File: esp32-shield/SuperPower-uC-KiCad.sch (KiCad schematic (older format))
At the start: 3 parts, among them J9 MCU board

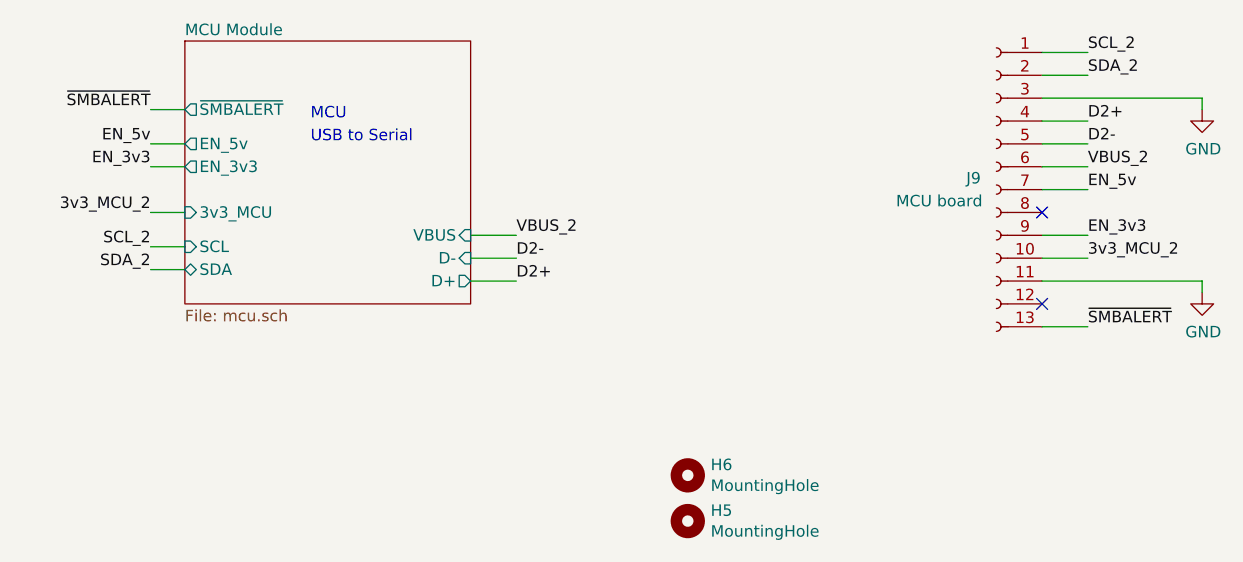
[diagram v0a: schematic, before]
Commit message: deleted unused files and renamed net lables
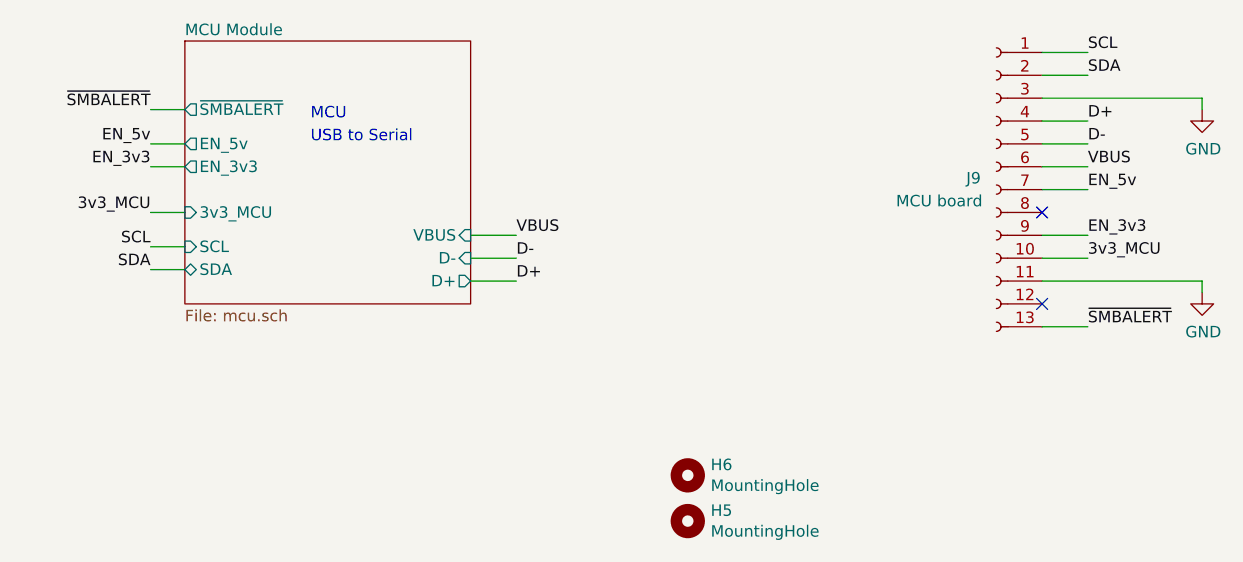
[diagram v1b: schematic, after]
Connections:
- net 3v3_MCU_2 renamed 3v3_MCU
- net D2+ renamed D+
- net D2- renamed D-
- net SCL_2 renamed SCL
- net SDA_2 renamed SDA
- net VBUS_2 renamed VBUS
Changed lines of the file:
@@
 USB to Serial
 Text Label 4500 3300 0    50   ~ 0
-VBUS_2
+VBUS
 Text Label 4500 3500 0    50   ~ 0
-D2+
+D+
 Text Label 4500 3400 0    50   ~ 0
-D2-
+D-
 Wire Wire Line
 	4500 3300 4300 3300
@@
 	4500 3500 4300 3500
 Text Label 2900 3200 2    50   ~ 0
-3v3_MCU_2
+3v3_MCU
 Text Label 2900 3350 2    50   ~ 0
-SCL_2
+SCL
 Text Label 2900 3450 2    50   ~ 0
-SDA_2
+SDA
 Wire Wire Line
 	2900 3450 3050 3450
@@
 	2900 3200 3050 3200
 Text Label 7000 3000 0    50   ~ 0
-VBUS_2
+VBUS
 Text Label 7000 2900 0    50   ~ 0
-D2-
+D-
 Wire Wire Line
 	7000 3000 6800 3000
@@
 	6800 2900 7000 2900
 Text Label 7000 3400 0    50   ~ 0
-3v3_MCU_2
+3v3_MCU
 Text Label 7000 2500 0    50   ~ 0
-SCL_2
+SCL
 Text Label 7000 2600 0    50   ~ 0
-SDA_2
+SDA
 Wire Wire Line
 	7000 2600 6800 2600
@@
 	7000 2800 6800 2800
 Text Label 7000 2800 0    50   ~ 0
-D2+
+D+
 $Comp
 L power:GND #PWR0111

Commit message: added rgbw led, swapped ch340g for ch340c part numers
also marked crystal and caps as DNP
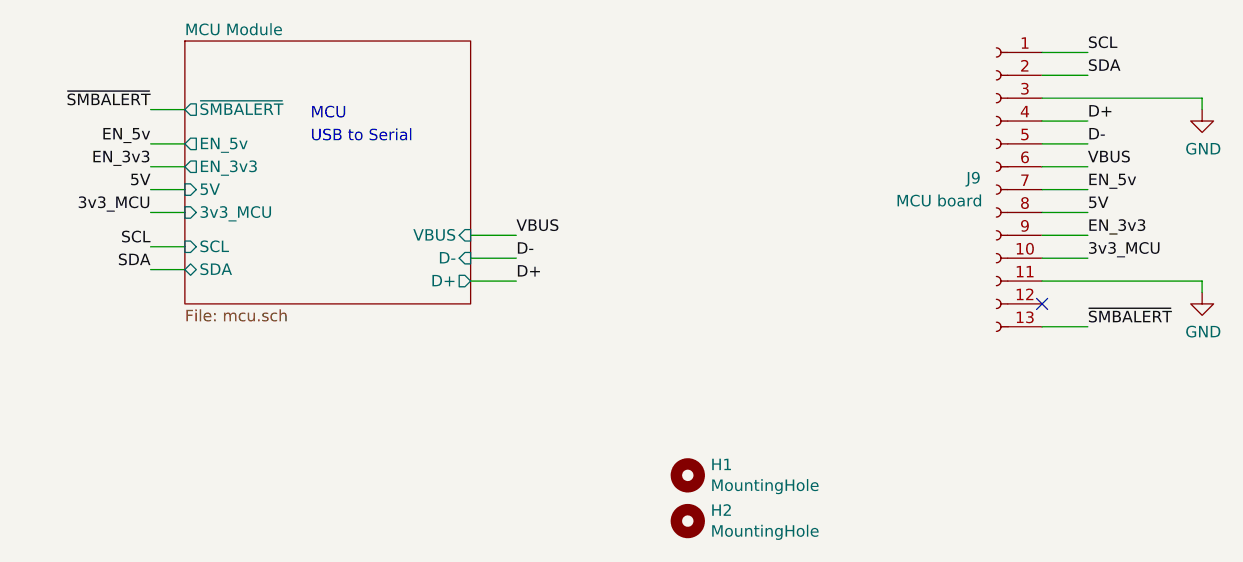
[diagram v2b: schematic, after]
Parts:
- renumbered H6 to H1, H5 to H2
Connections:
- net 5V: now reaches J9.8 (Pin_8)
- no-connect marks 2 -> 1
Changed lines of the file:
@@
 F9 "EN_5v" O L 3050 2900 50
 F10 "~SMBALERT" O L 3050 2750 50
+F11 "5V" I L 3050 3100 50
 $EndSheet
 Text Notes 3600 2800 0    50   ~ 0
@@
 Wire Wire Line
 	7500 2700 7500 2750
-NoConn ~ 6800 3200
 Wire Wire Line
 	6800 2700 7500 2700
@@
 	6800 3500 7500 3500
 $Comp
-L Mechanical:MountingHole H5
+L Mechanical:MountingHole H2
 U 1 1 60299211
 P 5250 4550
-F 0 "H5" H 5350 4596 50  0000 L CNN
+F 0 "H2" H 5350 4596 50  0000 L CNN
 F 1 "MountingHole" H 5350 4505 50  0000 L CNN
 F 2 "MountingHole:MountingHole_2.7mm_M2.5_ISO7380" H 5250 4550 50  0001 C CNN
@@
 $EndComp
 $Comp
-L Mechanical:MountingHole H6
+L Mechanical:MountingHole H1
 U 1 1 6029921B
 P 5250 4350
-F 0 "H6" H 5350 4396 50  0000 L CNN
+F 0 "H1" H 5350 4396 50  0000 L CNN
 F 1 "MountingHole" H 5350 4305 50  0000 L CNN
 F 2 "MountingHole:MountingHole_2.7mm_M2.5_ISO7380" H 5250 4350 50  0001 C CNN
@@
 	1    0    0    -1
 $EndComp
+Wire Wire Line
+	6800 3200 7000 3200
+Text Label 7000 3200 0    50   ~ 0
+5V
+Wire Wire Line
+	3050 3100 2900 3100
+Text Label 2900 3100 2    50   ~ 0
+5V
 $EndSCHEMATC

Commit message: swapped led for WS2812 footprint with logic level shifter
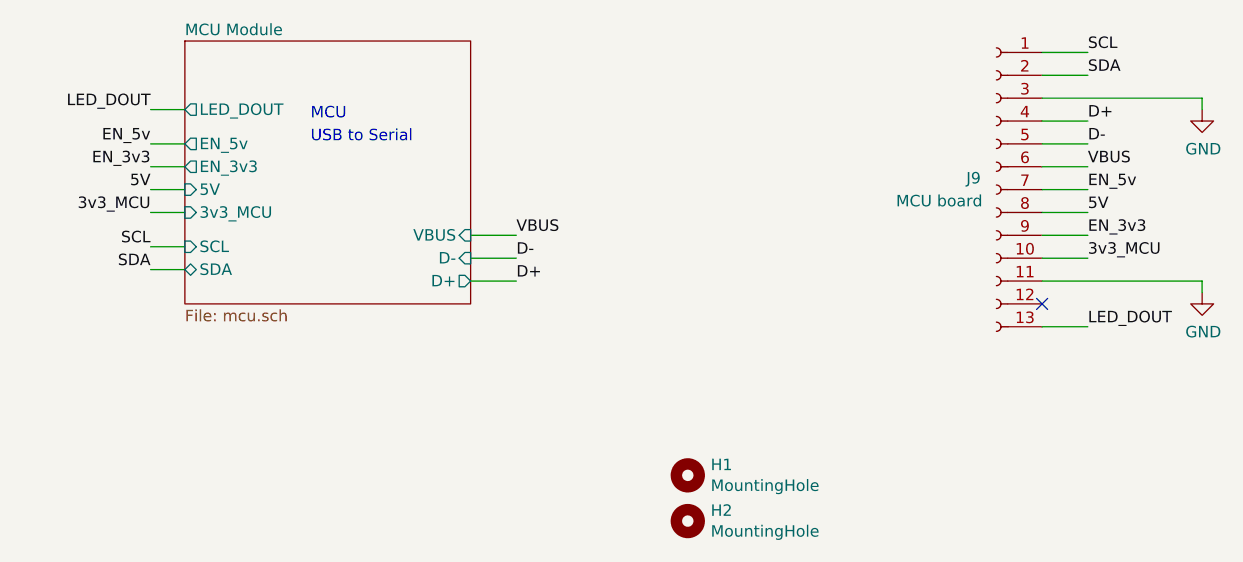
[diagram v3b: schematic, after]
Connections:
- net ~SMBALERT renamed LED_DOUT
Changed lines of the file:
@@
 Comment4 ""
 $EndDescr
-$Sheet
-S 3050 2450 1250 1150
-U 5F63A193
-F0 "MCU Module" 50
-F1 "mcu.sch" 50
-F2 "3v3_MCU" I L 3050 3200 50
-F3 "SDA" B L 3050 3450 50
-F4 "SCL" I L 3050 3350 50
-F5 "D+" O R 4300 3500 50
-F6 "D-" I R 4300 3400 50
-F7 "VBUS" I R 4300 3300 50
-F8 "EN_3v3" O L 3050 3000 50
-F9 "EN_5v" O L 3050 2900 50
-F10 "~SMBALERT" O L 3050 2750 50
-F11 "5V" I L 3050 3100 50
-$EndSheet
 Text Notes 3600 2800 0    50   ~ 0
 MCU
@@
 	2900 2750 3050 2750
 Text Label 2900 2750 2    50   ~ 0
-~SMBALERT
+LED_DOUT
 Text Label 2900 2900 2    50   ~ 0
 EN_5v
@@
 EN_3v3
 Text Label 7000 3700 0    50   ~ 0
-~SMBALERT
+LED_DOUT
 Text Label 7000 3100 0    50   ~ 0
 EN_5v
@@
 Text Label 2900 3100 2    50   ~ 0
 5V
+$Sheet
+S 3050 2450 1250 1150
+U 5F63A193
+F0 "MCU Module" 50
+F1 "mcu.sch" 50
+F2 "3v3_MCU" I L 3050 3200 50
+F3 "SDA" B L 3050 3450 50
+F4 "SCL" I L 3050 3350 50
+F5 "D+" O R 4300 3500 50
+F6 "D-" I R 4300 3400 50
+F7 "VBUS" I R 4300 3300 50
+F8 "EN_3v3" O L 3050 3000 50
+F9 "EN_5v" O L 3050 2900 50
+F11 "5V" I L 3050 3100 50
+F12 "LED_DOUT" O L 3050 2750 50
+$EndSheet
 $EndSCHEMATC
